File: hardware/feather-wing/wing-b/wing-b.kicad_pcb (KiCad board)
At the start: 2 copper layers, 50.8 x 27.9 mm, 27 parts, among them J1 USB-C plug, right angle, J2 Feather 16-pin, J3 Feather 12-pin, U2 AP22653W6-7, U3 USBLC6-2SC6, U4 USBLC6-2SC6

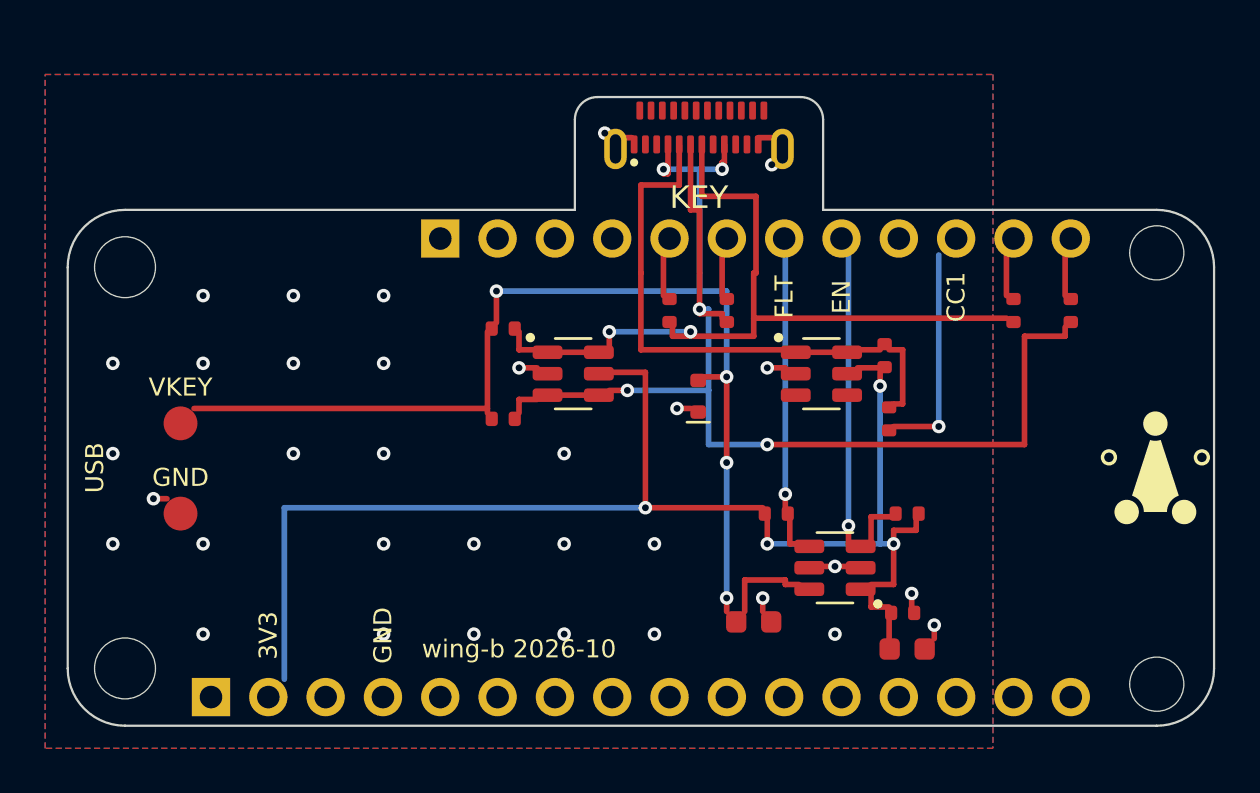
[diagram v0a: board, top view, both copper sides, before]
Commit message: wing-a and wing-b: KiCad-clean, key-c P3's LED line, wing-b on a straddle plug
KiCad 10.0.6 found what the self-check couldn't: gen_wing.py's rotate(),
shared with console-pocket, turned parts clockwise on the page where
KiCad turns them counter-clockwise, so every part at 90 or 270 had its
pads swapped against its tracks. rotate() is KiCad's now and ROT's 90s
and 270s are swapped; round pads join only inside their circle; loose
via and track ends are dropped. console-pocket's README now says not to
order it until it is regenerated the same way.

Both wings carry key-c P3's LED: A8 and B8 joined as KEY_LED, driven
from D13 (the status LED pin) through R13, D3 for ESD; R14 to A0 not
fitted. No firmware change.

wing-b is redrawn around a SHOU HAN 24P straddle-mount plug (C3151751)
on a tab out of the 12-pin side, in place of GCT's USB4155.

tools/keypcb fill then check, both wings: ERC 0, DRC 0, 0 unconnected,
parity clean. Fab files and renders in each wing's fab/. Not ordered.

Co-Authored-By: Claude Opus 5.5 <noreply@anthropic.com>
Claude-Session: https://claude.ai/code/session_014mGuGD4x9Si2dmdRKbhRec
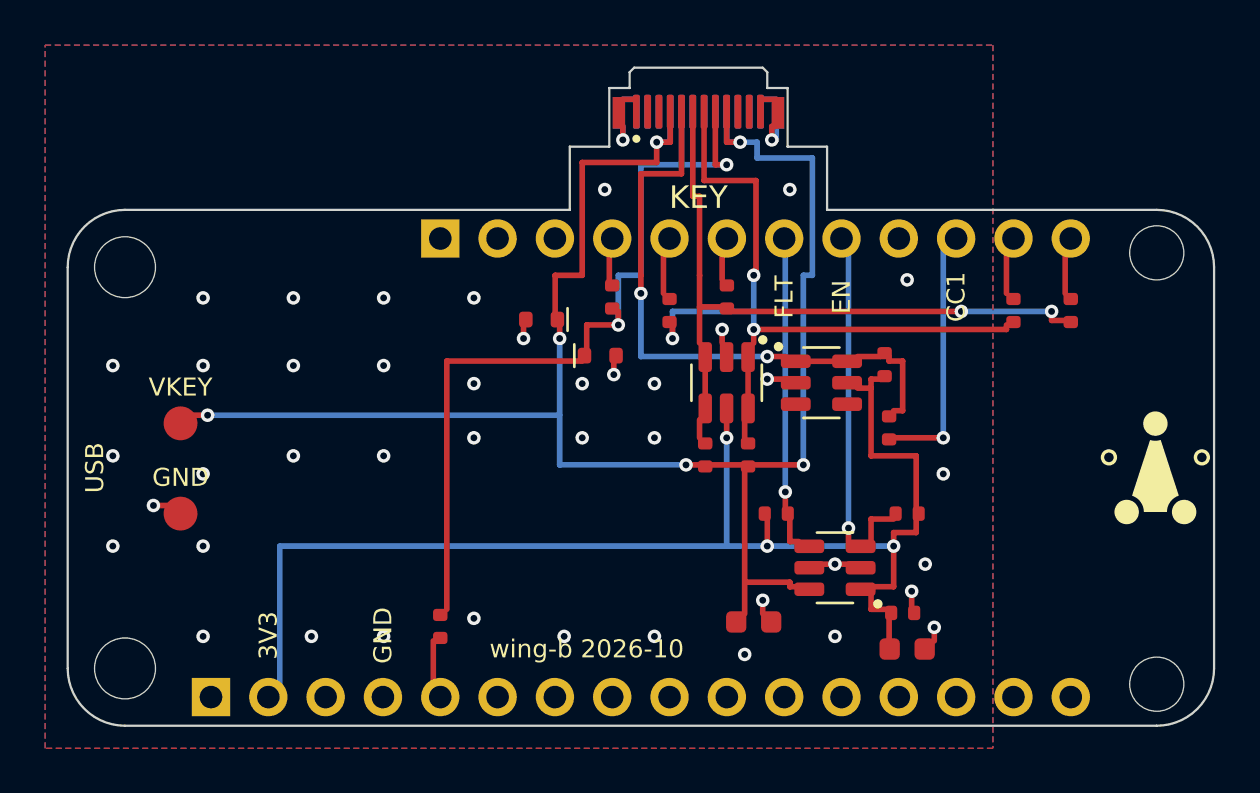
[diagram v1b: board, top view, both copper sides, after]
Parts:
- added D3: ESD5Z5V0, pqwing:D_SOD-523, F.Cu at (123.6, 123.6)
- added R13: 100, pqwing:R_0402, F.Cu at (124.1, 121.0)
- added R14: 100, pqwing:R_0402, F.Cu at (116.5, 135.6)
- J1: value USB-C plug, right angle -> USB-C plug, straddle mount; footprint pqwing:USB_C_Plug_GCT_USB4155_Horizontal -> pqwing:USB_C_Plug_ShouHan_24P-GTJB_Straddle
- moved R2 12.2 mm to (130.2, 128.0), turned to 90 degrees
- moved R1 9.09 mm to (128.2, 128.0), turned to 90 degrees
- moved D1 7.73 mm to (121.0, 122.0), turned to 180 degrees
- moved U3 6.81 mm to (129.2, 124.8), turned to -90 degrees
- moved J1 1.30 mm to (128.0, 110.8)
- moved R11 0.60 mm to (129.2, 121.0), turned to 90 degrees
- moved R3 0.40 mm to (136.2, 124.0), turned to 90 degrees
- moved R5 0.40 mm to (136.4, 126.8), turned to -90 degrees
- moved U4 0.40 mm to (133.4, 124.8)
- turned R10 to 90 degrees
- turned R12 to 90 degrees
- turned R9 to 90 degrees
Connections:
- J1 pad A8: unconnected-(J1-SBU1-PadA8) -> /KEY_LED
- J1 pad B1: unconnected-(J1-GND-PadB1) -> GND
- J1 pad B12: unconnected-(J1-GND-PadB12) -> GND
- J1 pad B4: unconnected-(J1-VBUS-PadB4) -> /VKEY
- J1 pad B8: unconnected-(J1-SBU2-PadB8) -> /KEY_LED
- J1 pad B9: unconnected-(J1-VBUS-PadB9) -> /VKEY
- J2 pad 5: unconnected-(J2-A0-Pad5) -> /LED_ALT
- J3 pad 4: unconnected-(J3-D13-Pad4) -> /LED_D13
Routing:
- net /KEY_LED: track 0.00 -> 37.3 mm, vias 0 -> 2
- net /VKEY: track 58.3 -> 79.5 mm
- net /KEY_SDA: track 44.6 -> 29.8 mm, vias 3 -> 2
- net GND: track 6.80 -> 11.8 mm, vias 33 -> 44
- net +3V3: track 59.2 -> 56.4 mm, vias 4 -> 3
- net /KEY_SCL: track 34.7 -> 32.5 mm, vias 2 -> 3
- net /LED_ALT: track 0.00 -> 2.00 mm
- net /CC1: track 23.9 -> 25.7 mm, vias 0 -> 2
- net /LED_D13: track 0.00 -> 1.40 mm
- net /CC1_SENSE: track 9.60 -> 10.6 mm
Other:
- board size 50.8 x 27.9 mm -> 50.8 x 29.2 mm
